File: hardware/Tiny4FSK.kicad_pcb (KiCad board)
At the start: 4 copper layers, 22 x 71 mm, 95 parts, among them J1 EXT_PWR, J2 GPIO, J3 I2C, J4 USB, J5 USB Breakout, J6 SPI, J7 GCT-4105, J8 SWD, J9 Counterpoise, SW1 PWR, SW2 RST, U1 BME280, U10 USBLC6-2SC6, U11 ATGM336H, U3 TPS61200DRC, U5 ATSAMD21G18A-A, U6 Si4463, U7 XC6210B332MR, U9 TPS2116DRL

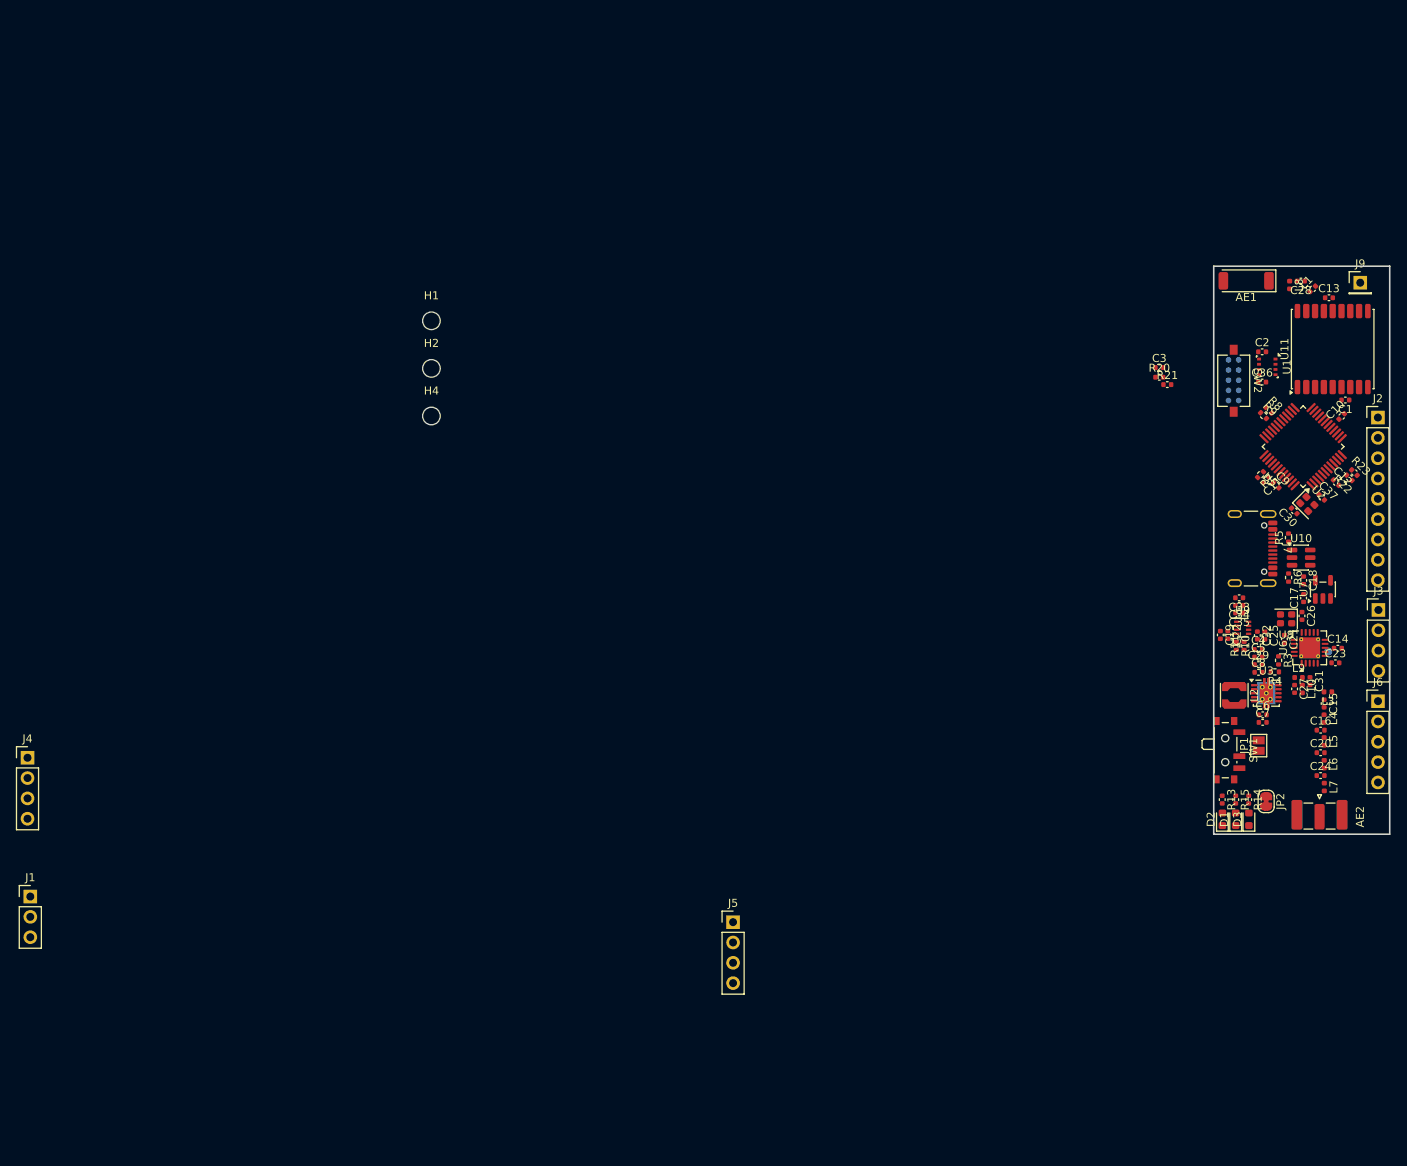
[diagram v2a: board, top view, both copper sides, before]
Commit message: lay out programming header + button, move powerpath near tx
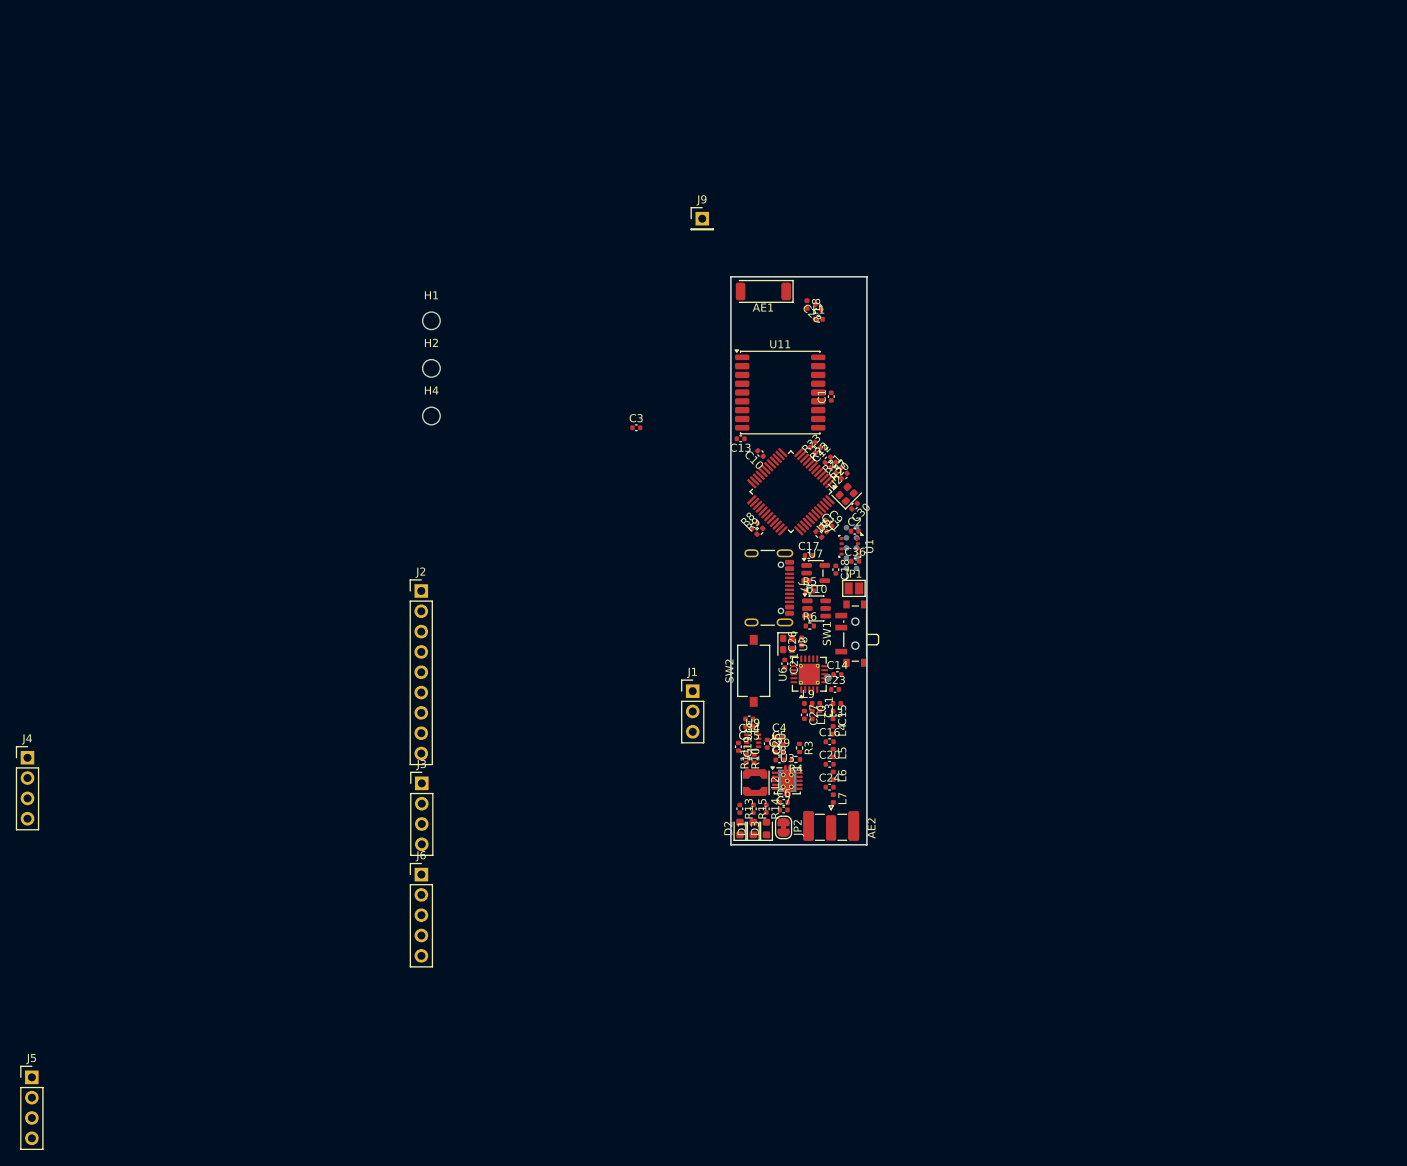
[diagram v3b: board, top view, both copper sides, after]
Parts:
- removed C22, C32, C33: 100nF, Capacitor_SMD:C_0402_1005Metric
- moved J2 121.5 mm to (91.3, 98.7)
- moved J3 121.5 mm to (91.4, 122.8)
- moved J6 121.5 mm to (91.3, 134.2)
- moved J5 89.8 mm to (42.6, 159.5)
- moved J1 86.7 mm to (125.2, 111.3)
- moved J9 82.6 mm to (126.4, 52.2)
- moved C13 75.6 mm to (131.2, 79.7), turned to 180 degrees
- moved C10 72.8 mm to (133.7, 81.6), turned to 135 degrees
- moved SW2 70.1 mm to (132.8, 108.7), turned to 90 degrees
- moved U11 69.3 mm to (136.2, 73.9), turned to 0 degrees
- moved R22 67.2 mm to (140.2, 80.5), turned to -135 degrees
- moved R23 67.1 mm to (140.9, 81.2), turned to 45 degrees
- moved R8 65.9 mm to (132.9, 90.6), turned to 45 degrees
- moved C3 65.8 mm to (118.2, 78.3)
- moved R9 64.6 mm to (133.6, 91.3), turned to 45 degrees
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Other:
- board size 22 x 71 mm -> 17 x 71 mm

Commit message: draft of gpio layout
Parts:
- removed J1: EXT_PWR, Connector_PinHeader_2.54mm:PinHeader_1x03_P2.54mm_Vertical
- removed J3: I2C, Connector_PinHeader_2.54mm:PinHeader_1x04_P2.54mm_Vertical
- removed J4: USB, Connector_PinHeader_2.54mm:PinHeader_1x04_P2.54mm_Vertical
- removed J6: SPI, Connector_PinHeader_2.54mm:PinHeader_1x05_P2.54mm_Vertical
- added J10: GPIO_ROW, Connector_PinHeader_2.54mm:PinHeader_1x15_P2.54mm_Vertical, F.Cu at (146.5, 71.4)
- J2: value GPIO -> PWR; footprint Connector_PinHeader_2.54mm:PinHeader_1x09_P2.54mm_Vertical -> Connector_PinHeader_2.54mm:PinHeader_1x06_P2.54mm_Vertical
- moved J2 48.2 mm to (130.1, 70.2)
- moved J8 36.9 mm to (108.3, 91.2)
- moved JP1 30.0 mm to (117.3, 109.2)
- moved U1 30.0 mm to (142.6, 63.3)
- moved C2 30.0 mm to (143.2, 61.4)
- moved C36 29.9 mm to (143.2, 65.2)
- moved SW1 22.3 mm to (130.0, 120.4), turned to -90 degrees
- moved C13 10.2 mm to (141.3, 81.0)
- moved C1 7.64 mm to (138.1, 68.2), turned to 180 degrees
- moved C26 5.20 mm to (134.9, 108.5)
- moved C35 3.75 mm to (134.6, 112.8)
- moved C25 3.56 mm to (136.9, 115.2), turned to 90 degrees
- moved SW2 3.38 mm to (130.4, 111.0)
- moved U8 3.17 mm to (136.9, 108.5), turned to 0 degrees
- moved C19 3.07 mm to (133.3, 116.2)
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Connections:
- J2 pad 1: /interface/GP.GPIO38 -> Earth
- J2 pad 2: Earth -> +BATT
- J2 pad 3: /interface/GP.GPIO12 -> Earth
- J2 pad 4: Earth -> +3.3V
- J2 pad 5: /interface/GP.GPIO13 -> Earth
- J2 pad 6: Earth -> +3.3V
- JP1 pad 1: +BATT -> /power/BST_IN
- JP1 pad 2: /power/BST_IN -> +BATT
- SW1 pad 1: /power/BST_IN -> +BATT
- SW1 pad 2: +BATT -> /power/BST_IN
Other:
- board size 17 x 71 mm -> 20 x 71 mm

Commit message: draft of final layout
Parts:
- removed C29: 100nF, Capacitor_SMD:C_0402_1005Metric
- SW2: footprint Button_Switch_SMD:SW_Tactile_SPST_NO_Straight_CK_PTS636Sx25SMTRLFS -> Button_Switch_SMD:SW_SPST_TS-1088-xR020
- moved H4 75.8 mm to (158.6, 114.2)
- moved H1 72.2 mm to (137.7, 121.3)
- moved H2 53.1 mm to (145.5, 67.0)
- moved J8 22.3 mm to (130.5, 89.9), turned to 0 degrees
- moved SW2 18.1 mm to (142.8, 97.8)
- moved JP1 16.8 mm to (134.0, 107.0), turned to 180 degrees
- moved R8 14.7 mm to (142.9, 83.5), turned to -135 degrees
- moved R9 14.6 mm to (142.2, 82.8), turned to -135 degrees
- moved C10 12.7 mm to (141.4, 92.6), turned to -135 degrees
- moved U2 12.4 mm to (130.6, 88.2), turned to -135 degrees
- moved C37 11.8 mm to (131.7, 89.6), turned to -135 degrees
- moved R7 11.7 mm to (134.6, 82.8), turned to 135 degrees
- moved C30 11.5 mm to (132.6, 85.4), turned to -135 degrees
- moved C11 11.1 mm to (133.9, 83.5), turned to 135 degrees
- moved SW1 11.1 mm to (129.9, 109.3)
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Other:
- board size 20 x 71 mm -> 20 x 63 mm

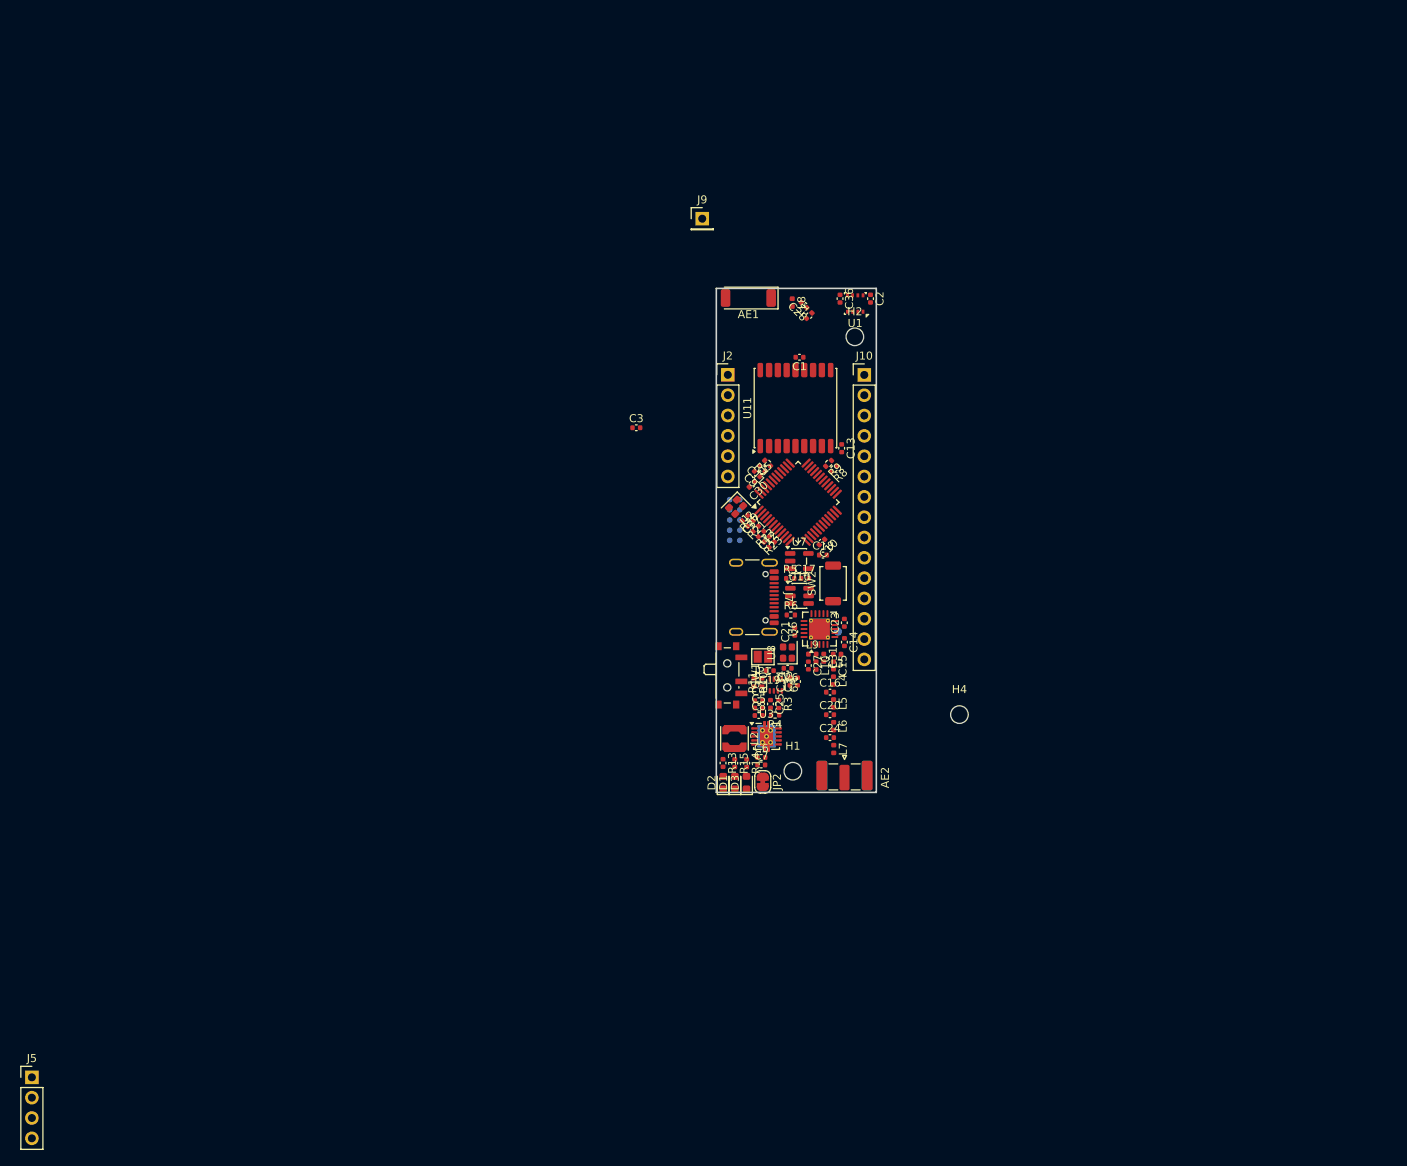
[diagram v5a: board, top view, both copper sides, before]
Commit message: layout bk-53 and adjust layout
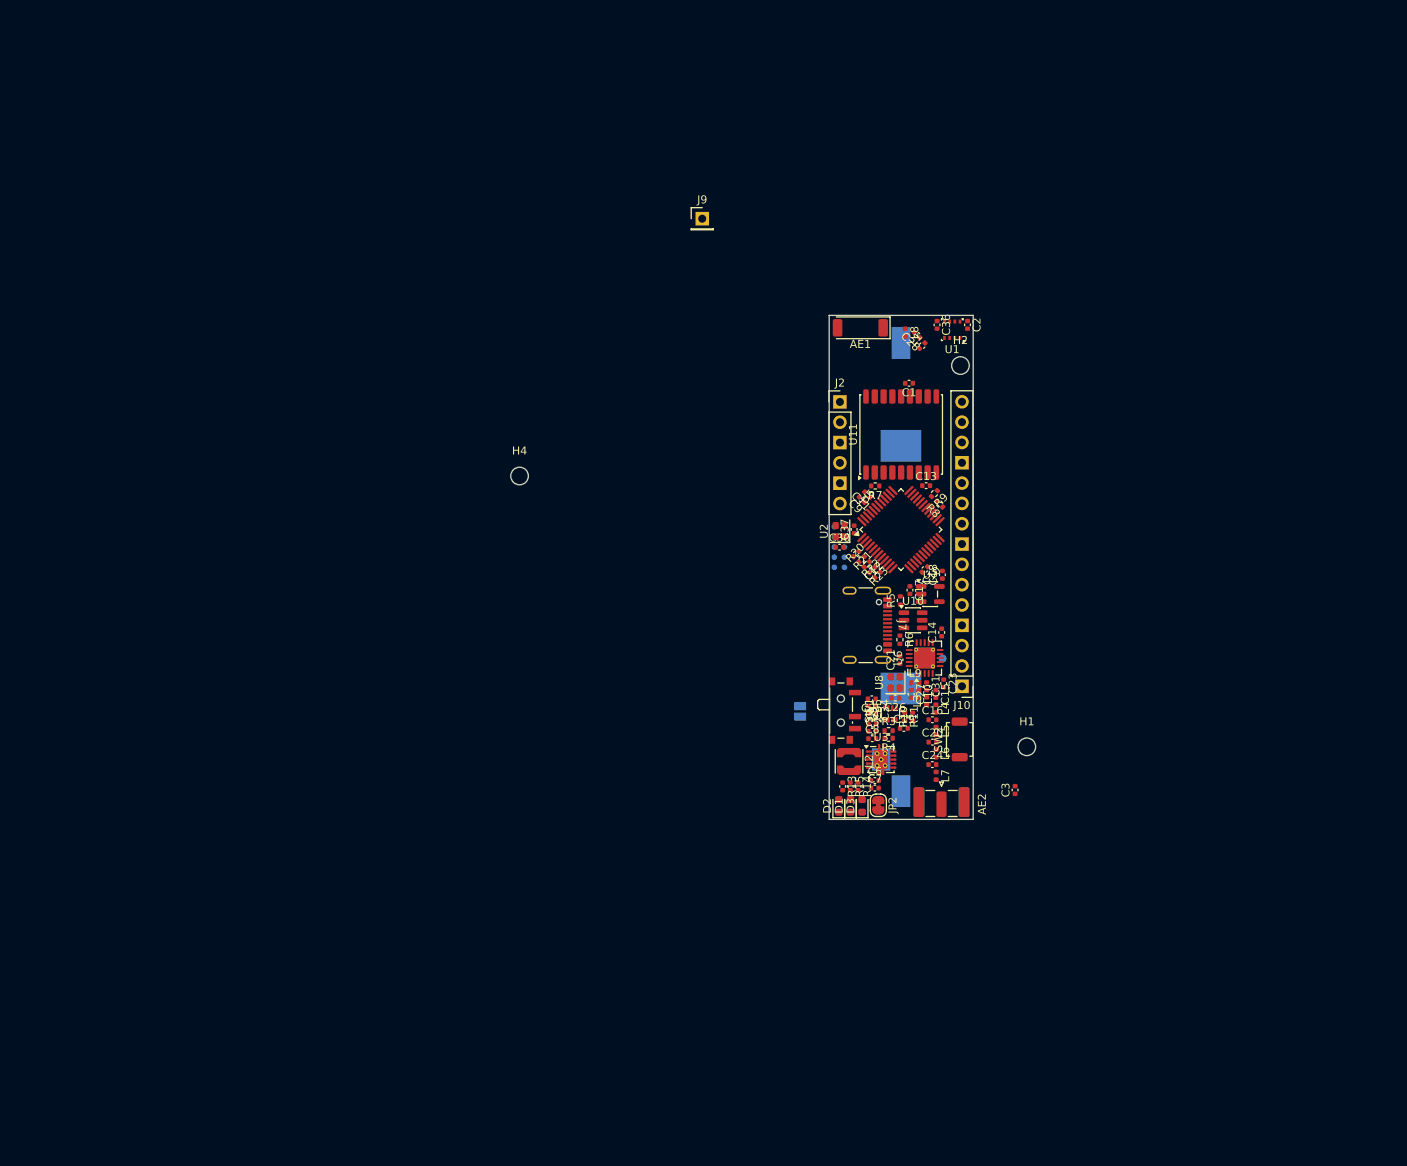
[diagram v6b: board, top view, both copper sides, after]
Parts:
- removed J5: USB Breakout, Connector_PinHeader_2.54mm:PinHeader_1x04_P2.54mm_Vertical
- added BT1: BK-53, Battery_Custom:BAT_BK-53, B.Cu at (151.2, 95.8)
- JP1: moved to B.Cu
- moved C3 65.5 mm to (165.5, 123.6), turned to 90 degrees
- moved H4 62.6 mm to (103.6, 84.4)
- moved J10 40.8 mm to (158.9, 110.7), turned to 180 degrees
- moved H1 29.4 mm to (167.0, 118.2)
- moved SW2 25.1 mm to (158.6, 117.3)
- moved R10 20.3 mm to (152.7, 114.5), turned to 90 degrees
- moved R11 18.4 mm to (151.7, 114.5), turned to -90 degrees
- moved C19 18.3 mm to (151.6, 115.9), turned to 0 degrees
- moved U7 16.9 mm to (154.9, 99.1)
- moved R13 15.2 mm to (144.0, 123.2)
- moved C18 15.1 mm to (156.4, 96.7), turned to 90 degrees
- moved SW1 14.9 mm to (144.1, 113.7)
- moved U9 14.8 mm to (149.9, 114.1), turned to 90 degrees
- moved JP2 14.7 mm to (148.4, 125.5)
- moved D2 14.7 mm to (143.5, 125.6)
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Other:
- board size 20 x 63 mm -> 18 x 63 mm

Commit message: net class shenanigans
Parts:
- moved C3 14.2 mm to (151.3, 123.6)
- moved C2 12.8 mm to (146.8, 65.5)
- moved C36 12.8 mm to (143.0, 65.5)
- moved U1 12.8 mm to (144.9, 66.1)
- moved JP1 6.90 mm to (145.5, 113.0)
- moved C19 4.18 mm to (147.4, 115.9)
- moved C34 4.18 mm to (143.9, 113.6)
- moved C35 4.18 mm to (143.0, 113.6)
- moved R10 4.18 mm to (148.5, 114.5)
- moved U9 4.18 mm to (145.7, 114.1)
- moved C25 4.18 mm to (143.4, 112.2)
- moved R11 4.18 mm to (147.5, 114.5)
- moved SW2 1.58 mm to (158.6, 115.7)
- moved J8 0.58 mm to (144.1, 93.2)
- moved TP1 0.48 mm to (156.6, 107.7)
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
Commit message: more placement
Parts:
- moved H1 38.7 mm to (173.4, 80.0)
- moved C2 12.6 mm to (159.4, 65.5)
- moved C36 12.6 mm to (155.6, 65.5)
- moved U1 12.6 mm to (157.5, 66.1)
- moved C30 5.26 mm to (139.6, 96.5), turned to -90 degrees
- moved AE1 3.34 mm to (143.9, 68.3), turned to -90 degrees
- moved U2 3.20 mm to (140.7, 92.1), turned to 0 degrees
- moved C37 2.57 mm to (144.6, 93.5), turned to -135 degrees
- moved R22 0.70 mm to (148.3, 97.2), turned to 0 degrees
- moved L7 0.45 mm to (156.1, 121.7), turned to -45 degrees
- moved C12 0.44 mm to (146.6, 95.5)
- moved R23 0.43 mm to (147.3, 96.2)
- moved R20 0.42 mm to (145.9, 94.8)
- moved R21 0.41 mm to (145.3, 94.1)
- moved U5 0.37 mm to (151.2, 91.4)
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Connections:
- net /sensors/ANT_GPS renamed Net-(U11-RF_IN)
- net Net-(J7-D+-PadA6) renamed /power/RAW.D+
- net Net-(J7-D--PadA7) renamed /power/RAW.D-
